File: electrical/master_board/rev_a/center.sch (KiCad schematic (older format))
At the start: 4 parts

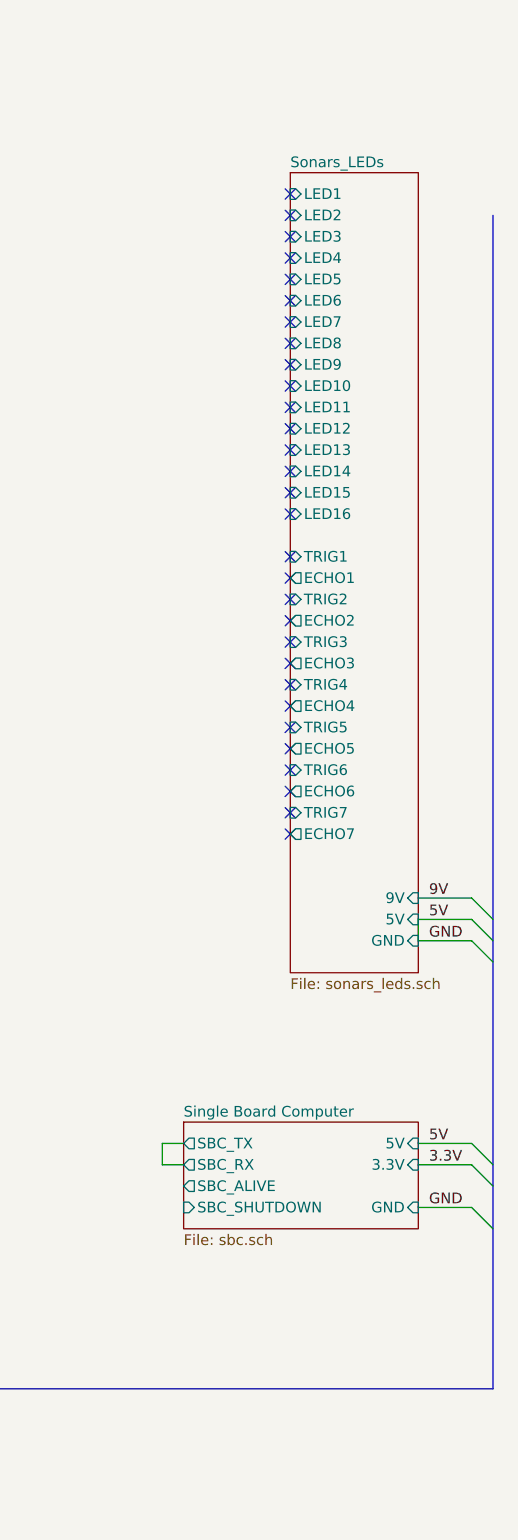
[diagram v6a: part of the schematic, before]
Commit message: Added level shifting to Sonars.  Added shift register for LED's.
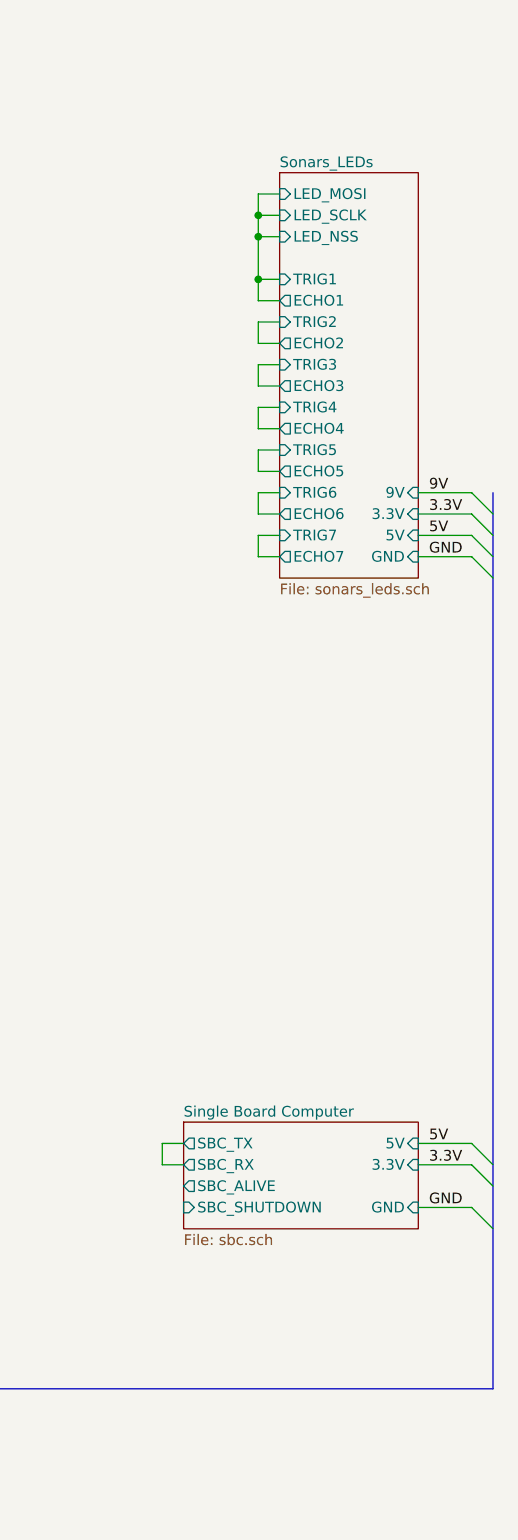
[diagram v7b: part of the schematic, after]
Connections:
- no-connect marks 43 -> 13
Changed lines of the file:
@@
 $EndSheet
 NoConn ~ 5950 -150
-NoConn ~ 8050 900
-NoConn ~ 8050 1000
-NoConn ~ 8050 1100
-NoConn ~ 8050 1200
-NoConn ~ 8050 1300
-NoConn ~ 8050 1400
-NoConn ~ 8050 1500
-NoConn ~ 8050 1600
-NoConn ~ 8050 1700
-NoConn ~ 8050 1800
-NoConn ~ 8050 1900
-NoConn ~ 8050 2000
-NoConn ~ 8050 2100
-NoConn ~ 8050 2200
-NoConn ~ 8050 2300
-NoConn ~ 8050 2400
-NoConn ~ 8050 2600
-NoConn ~ 8050 2700
-NoConn ~ 8050 2800
-NoConn ~ 8050 2900
-NoConn ~ 8050 3000
-NoConn ~ 8050 3100
-NoConn ~ 8050 3200
-NoConn ~ 8050 3300
-NoConn ~ 8050 3400
-NoConn ~ 8050 3500
-NoConn ~ 8050 3600
-NoConn ~ 8050 3700
-$Sheet
-S 8050 800  600  3750
-U 5F48CAAD
-F0 "Sonars_LEDs" 50
-F1 "sonars_leds.sch" 50
-F2 "LED1" I L 8050 900 50
-F3 "LED2" I L 8050 1000 50
-F4 "LED3" I L 8050 1100 50
-F5 "LED4" I L 8050 1200 50
-F6 "LED5" I L 8050 1300 50
-F7 "LED6" I L 8050 1400 50
-F8 "LED7" I L 8050 1500 50
-F9 "LED8" I L 8050 1600 50
-F10 "LED9" I L 8050 1700 50
-F11 "LED10" I L 8050 1800 50
-F12 "LED11" I L 8050 1900 50
-F13 "LED12" I L 8050 2000 50
-F14 "LED13" I L 8050 2100 50
-F15 "LED14" I L 8050 2200 50
-F16 "LED15" I L 8050 2300 50
-F17 "LED16" I L 8050 2400 50
-F18 "TRIG2" I L 8050 2800 50
-F19 "ECHO2" O L 8050 2900 50
-F20 "TRIG3" I L 8050 3000 50
-F21 "ECHO3" O L 8050 3100 50
-F22 "TRIG4" I L 8050 3200 50
-F23 "ECHO4" O L 8050 3300 50
-F24 "TRIG5" I L 8050 3400 50
-F25 "ECHO5" O L 8050 3500 50
-F26 "TRIG6" I L 8050 3600 50
-F27 "ECHO6" O L 8050 3700 50
-F28 "TRIG7" I L 8050 3800 50
-F29 "ECHO7" O L 8050 3900 50
-F30 "9V" I R 8650 4200 50
-F31 "5V" I R 8650 4300 50
-F32 "GND" I R 8650 4400 50
-F33 "TRIG1" I L 8050 2600 50
-F34 "ECHO1" O L 8050 2700 50
-$EndSheet
 $Sheet
 S 1150 5500 800  600
@@
 F5 "3.3V" O L 1150 5800 50
 $EndSheet
-NoConn ~ 8050 3800
-NoConn ~ 8050 3900
 $Sheet
 S 4900 1750 1200 700
@@
 GND
 Wire Wire Line
-	8650 4200 8900 4200
-Wire Wire Line
-	8650 4300 8650 4400
-Wire Wire Line
-	8650 4400 8900 4400
-Wire Wire Line
-	8650 4300 8900 4300
-Entry Wire Line
-	8900 4200 9000 4300
-Entry Wire Line
-	8900 4300 9000 4400
-Entry Wire Line
-	8900 4400 9000 4500
-Text Label 8700 4200 0    50   ~ 0
+	8650 2400 8900 2400
+Wire Wire Line
+	8650 2600 8900 2600
+Wire Wire Line
+	8650 2500 8900 2500
+Entry Wire Line
+	8900 2400 9000 2500
+Entry Wire Line
+	8900 2500 9000 2600
+Entry Wire Line
+	8900 2600 9000 2700
+Text Label 8700 2300 0    50   ~ 0
 9V
-Text Label 8700 4300 0    50   ~ 0
+Text Label 8700 2500 0    50   ~ 0
 5V
-Text Label 8700 4400 0    50   ~ 0
+Text Label 8700 2600 0    50   ~ 0
 GND
 Wire Wire Line
@@
 Wire Wire Line
 	7450 5450 7550 5450
+$Sheet
+S 8000 800  650  1900
+U 5F48CAAD
+F0 "Sonars_LEDs" 50
+F1 "sonars_leds.sch" 50
+F2 "TRIG2" I L 8000 1500 50
+F3 "ECHO2" O L 8000 1600 50
+F4 "TRIG3" I L 8000 1700 50
+F5 "ECHO3" O L 8000 1800 50
+F6 "TRIG4" I L 8000 1900 50
+F7 "ECHO4" O L 8000 2000 50
+F8 "TRIG5" I L 8000 2100 50
+F9 "ECHO5" O L 8000 2200 50
+F10 "TRIG6" I L 8000 2300 50
+F11 "ECHO6" O L 8000 2400 50
+F12 "TRIG7" I L 8000 2500 50
+F13 "ECHO7" O L 8000 2600 50
+F14 "9V" I R 8650 2300 50
+F15 "5V" I R 8650 2500 50
+F16 "GND" I R 8650 2600 50
+F17 "TRIG1" I L 8000 1300 50
+F18 "ECHO1" O L 8000 1400 50
+F19 "LED_MOSI" I L 8000 900 50
+F20 "LED_SCLK" I L 8000 1000 50
+F21 "LED_NSS" I L 8000 1100 50
+F22 "3.3V" I R 8650 2400 50
+$EndSheet
+Wire Wire Line
+	8650 2300 8900 2300
+Entry Wire Line
+	8900 2300 9000 2400
+Text Label 8700 2400 0    50   ~ 0
+3.3V
+Wire Wire Line
+	8000 1300 7900 1300
+Wire Wire Line
+	7900 1300 7900 1400
+Wire Wire Line
+	7900 1400 8000 1400
+Wire Wire Line
+	8000 1500 7900 1500
+Wire Wire Line
+	7900 1500 7900 1600
+Wire Wire Line
+	7900 1600 8000 1600
+Wire Wire Line
+	8000 1700 7900 1700
+Wire Wire Line
+	7900 1700 7900 1800
+Wire Wire Line
+	7900 1800 8000 1800
+Wire Wire Line
+	8000 2000 7900 2000
+Wire Wire Line
+	7900 2000 7900 1900
+Wire Wire Line
+	7900 1900 8000 1900
+Wire Wire Line
+	8000 2200 7900 2200
+Wire Wire Line
+	7900 2200 7900 2100
+Wire Wire Line
+	7900 2100 8000 2100
+Wire Wire Line
+	8000 2400 7900 2400
+Wire Wire Line
+	7900 2400 7900 2300
+Wire Wire Line
+	7900 2300 8000 2300
+Wire Wire Line
+	8000 2600 7900 2600
+Wire Wire Line
+	7900 2600 7900 2500
+Wire Wire Line
+	7900 2500 8000 2500
+Wire Wire Line
+	7900 1300 7900 1100
+Wire Wire Line
+	7900 1100 8000 1100
+Connection ~ 7900 1300
+Wire Wire Line
+	7900 1100 7900 1000
+Wire Wire Line
+	7900 1000 8000 1000
+Connection ~ 7900 1100
+Wire Wire Line
+	7900 1000 7900 900
+Wire Wire Line
+	7900 900  8000 900
+Connection ~ 7900 1000
 Wire Bus Line
 	800  1700 800  6500
 Wire Bus Line
-	9000 1000 9000 6500
+	9000 2300 9000 6500
 $EndSCHEMATC

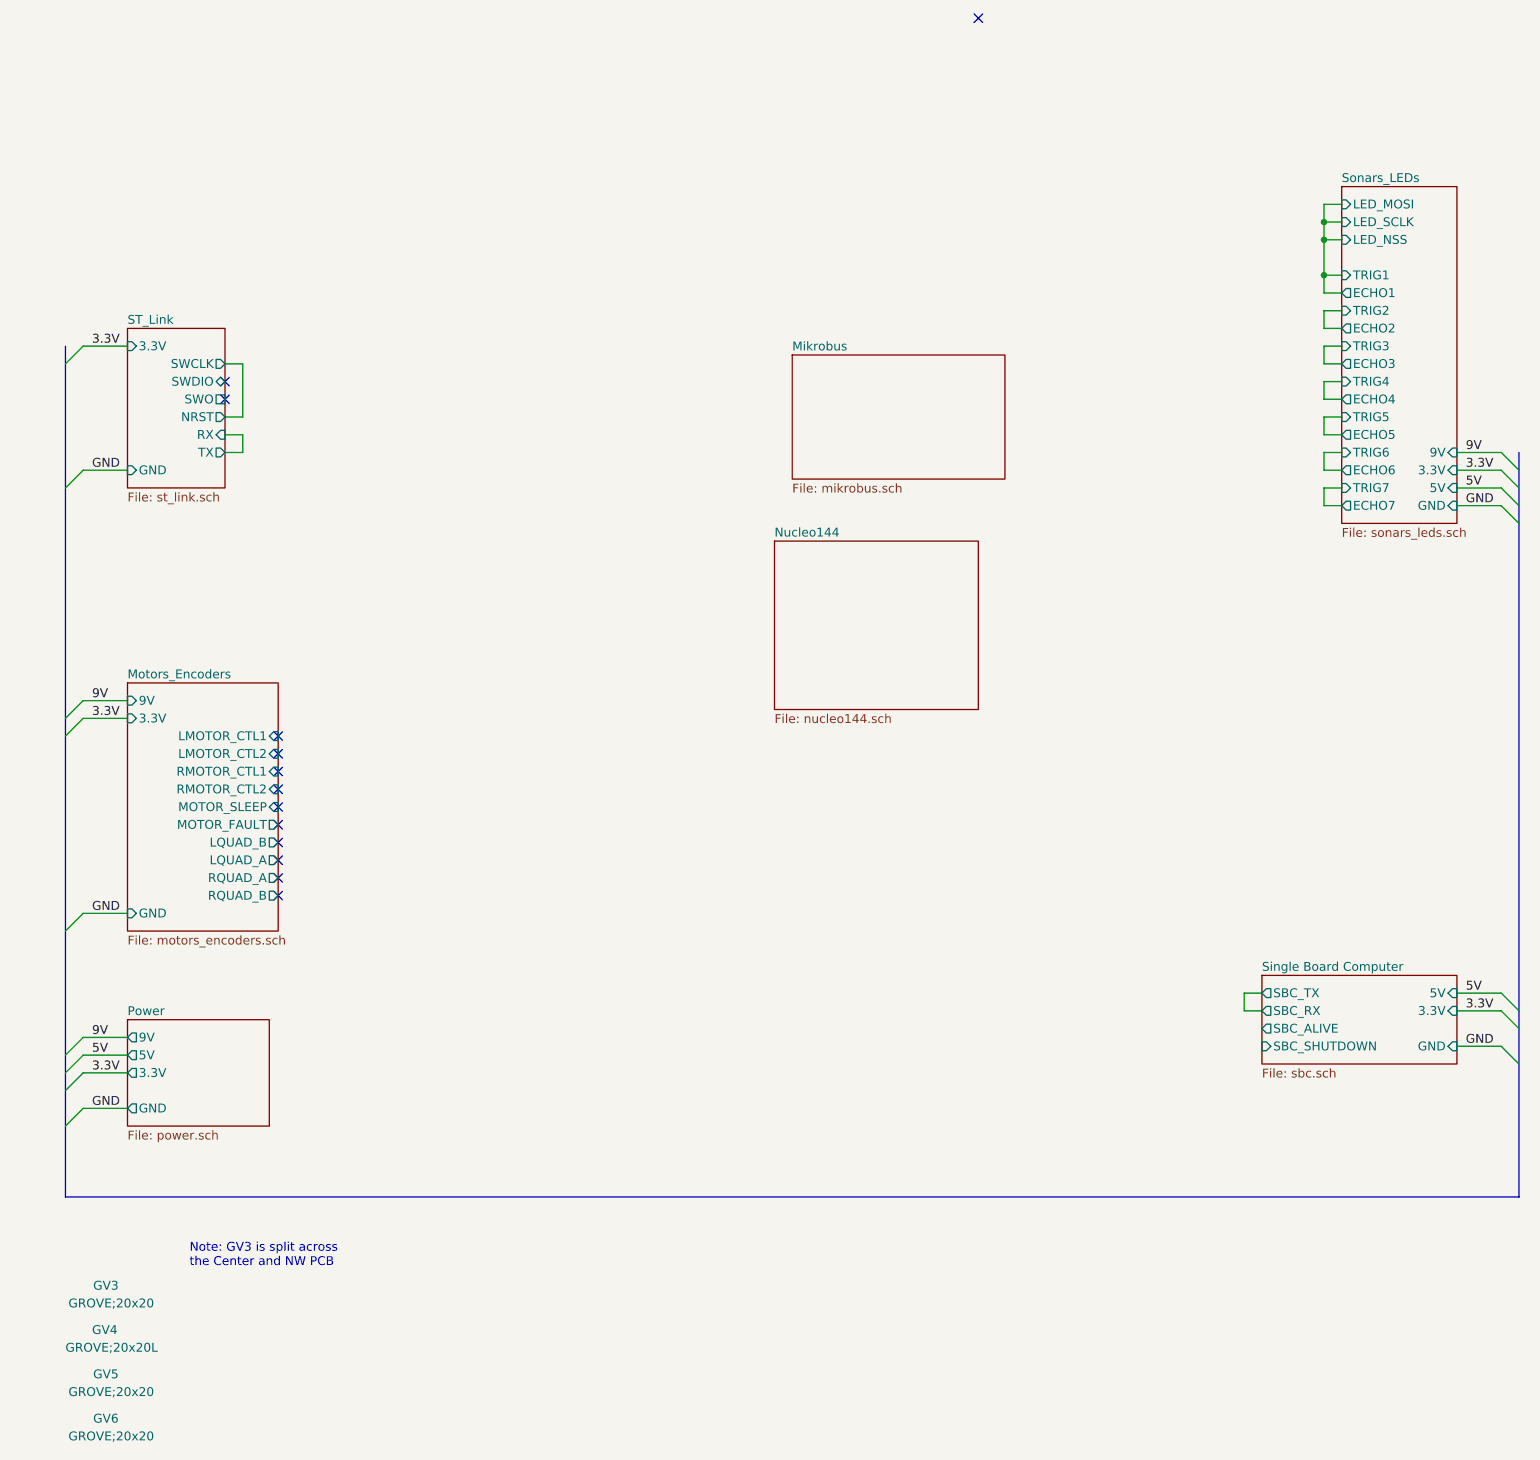
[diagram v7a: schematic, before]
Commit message: Added servo connectors.
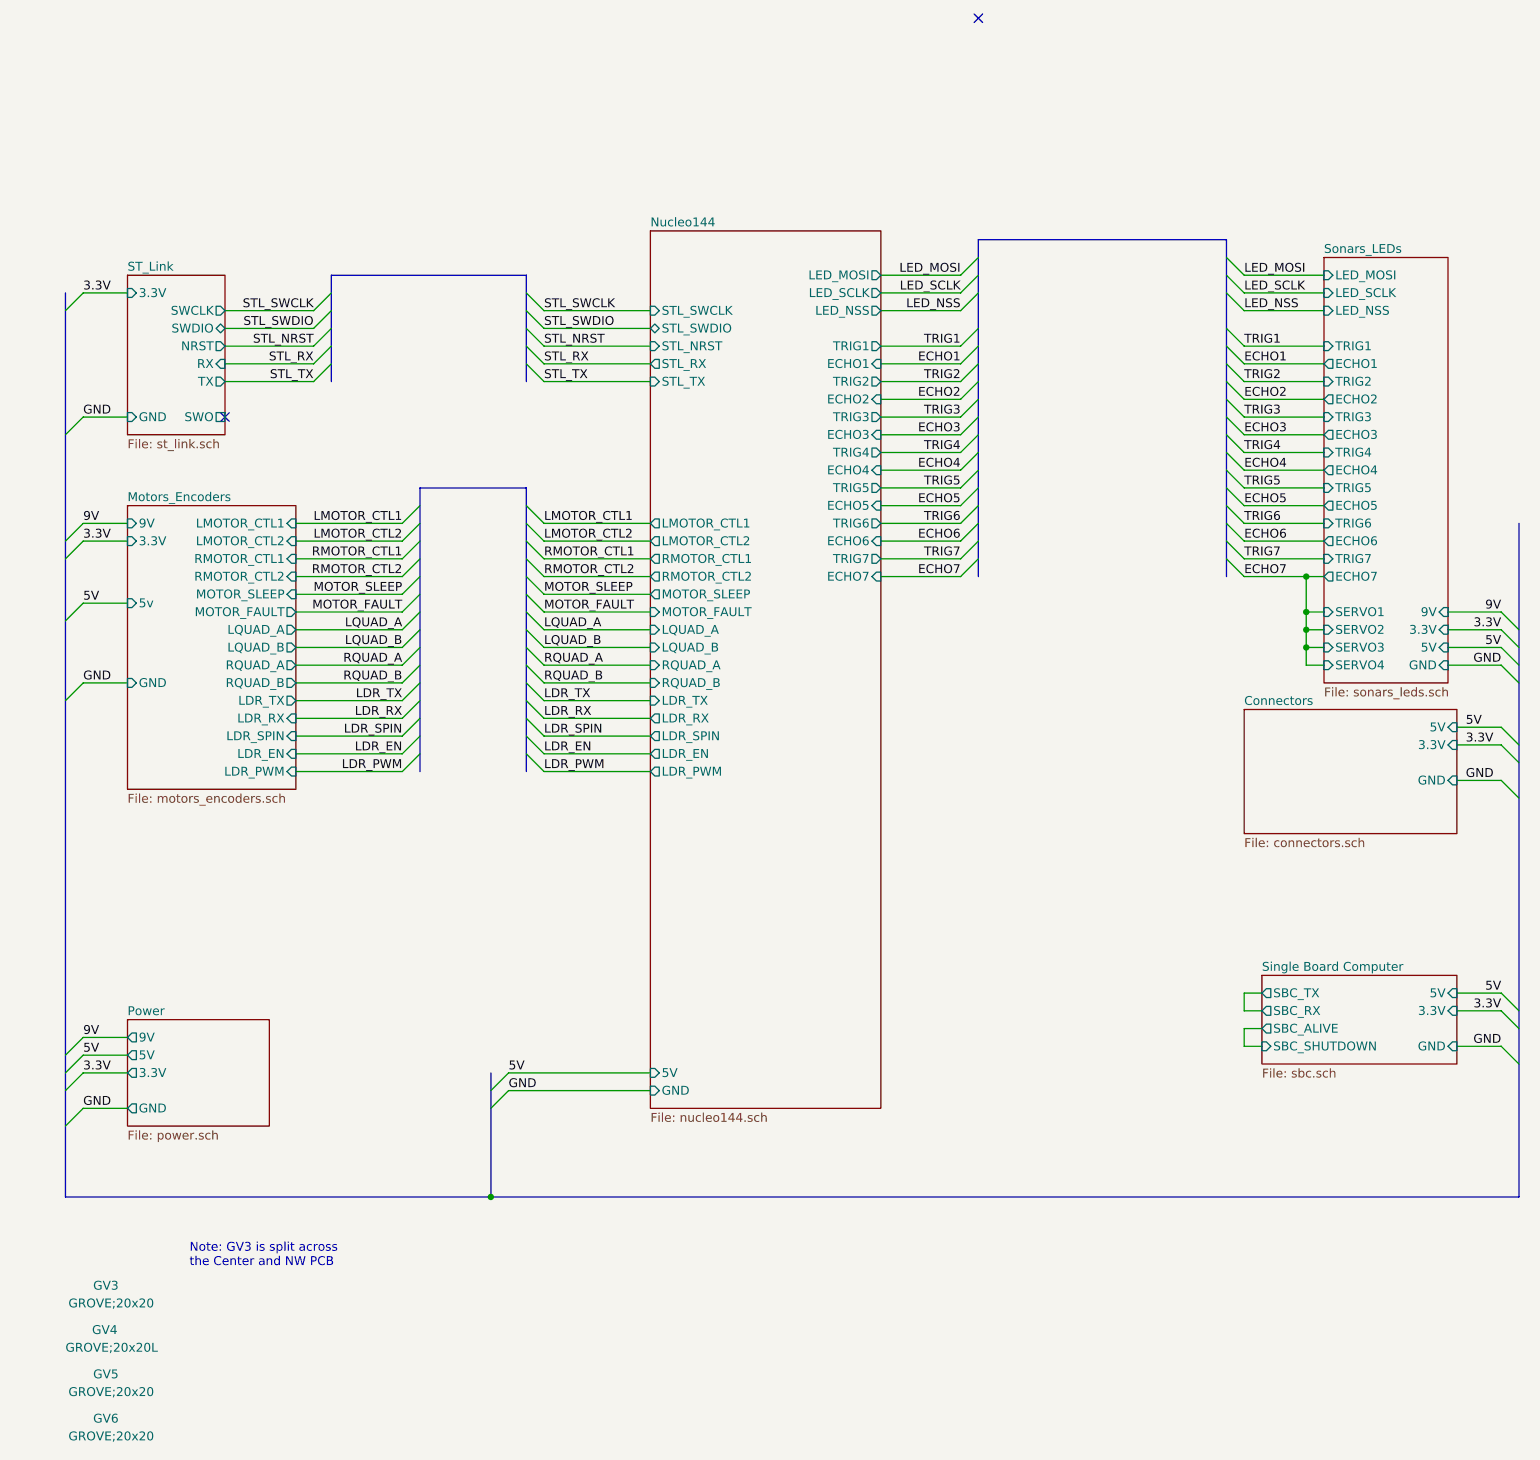
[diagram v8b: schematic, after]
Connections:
- no-connect marks 13 -> 2
